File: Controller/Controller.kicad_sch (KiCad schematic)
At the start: 27 parts, among them SW1 SW_DPST_x2, SW2 SW_Push, SW3 SW_Push, SW4 SW_Push, SW5 SW_Push, SW6 SW_Push, SW7 SW_Push, SW8 SW_Push, SW9 SW_Push

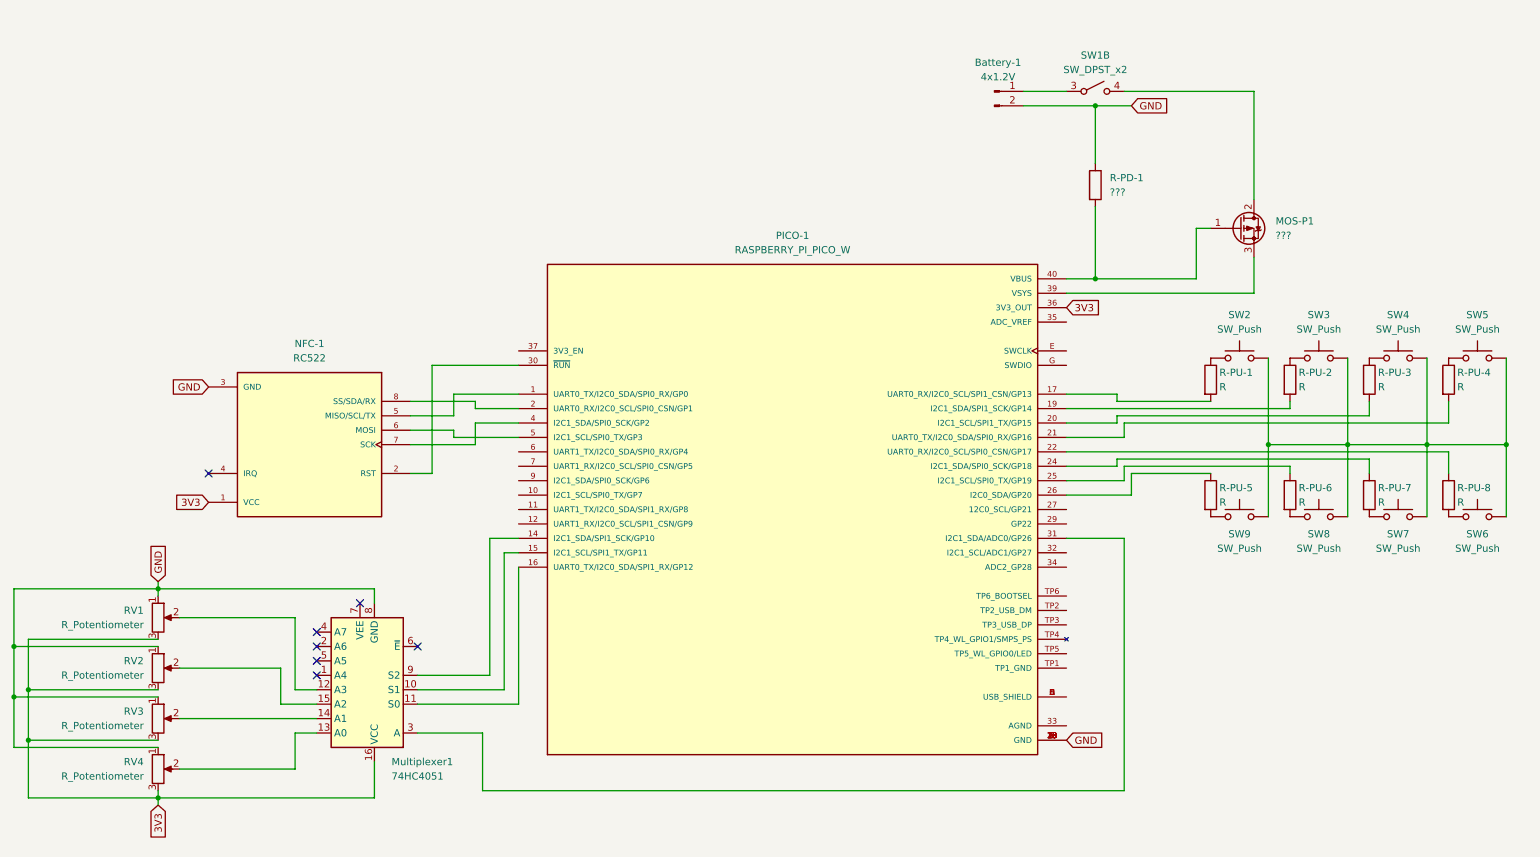
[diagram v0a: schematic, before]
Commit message: Add LEDs and fix button pull up resistors
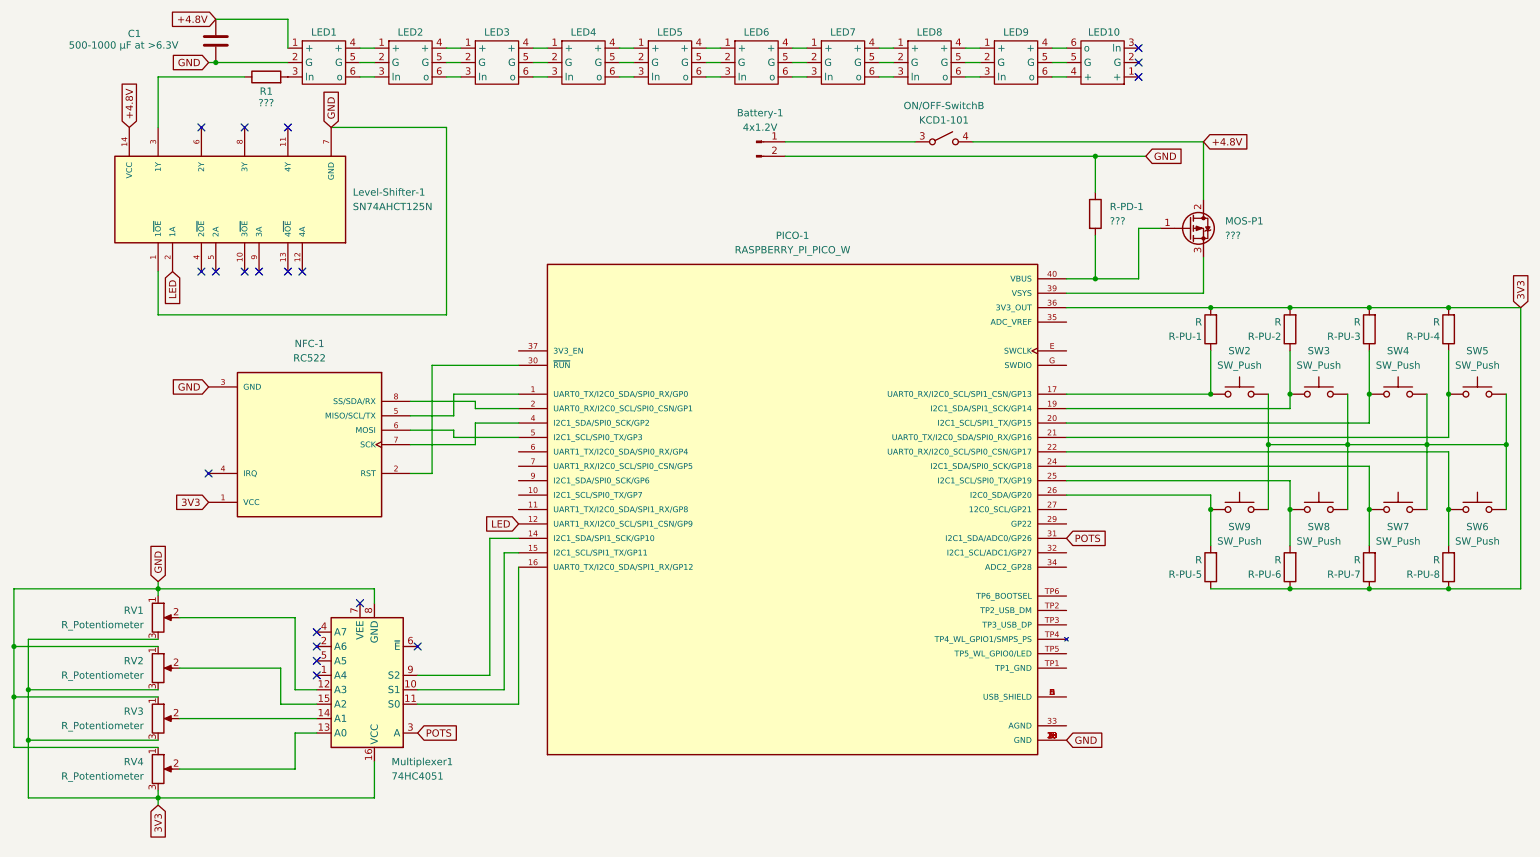
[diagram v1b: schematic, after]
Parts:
- added C1: 500-1000 μF at >6.3V, symbol Device:C
- added LED1, LED10, LED2, LED3, LED4, LED5, LED6, LED7, LED8, LED9: ~, symbol neopixel:neopixel_rgb_pcb
- added Level-Shifter-1: SN74AHCT125N, SN74AHCT125N:DIP794W45P254L1930H508Q14, symbol SN74AHCT125N:SN74AHCT125N
- added R1: ???, symbol Device:R
- NFC-1: footprint Connector_PinHeader_1.00mm:PinHeader_1x08_P1.00mm_Vertical -> CEG006900:MODULE_CEG006900
- ON/OFF-Switch: renamed from SW1; value SW_DPST_x2 -> KCD1-101
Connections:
- net 3V3: now also R-PU-1.2, R-PU-2.2, R-PU-3.2, R-PU-4.2, R-PU-5.1, R-PU-6.1, R-PU-7.1, R-PU-8.1
- net GND: now also C1.2, LED1.2 (G), Level-Shifter-1.1 (1~{OE}), Level-Shifter-1.7 (GND)
- net LED: now reaches PICO-1.12 (UART1_RX/I2C0_SCL/SPI1_CSN/GP9)
- net LED: now also Level-Shifter-1.2 (1A)
- net at PICO-1.17 (UART0_RX/I2C0_SCL/SPI1_CSN/GP13): now also R-PU-1.1, SW2.1; no longer R-PU-1.2
- net at PICO-1.19 (I2C1_SDA/SPI1_SCK/GP14): now also R-PU-2.1, SW3.1; no longer R-PU-2.2
- net at PICO-1.20 (I2C1_SCL/SPI1_TX/GP15): now also R-PU-3.1, SW4.1; no longer R-PU-3.2
- net at PICO-1.21 (UART0_TX/I2C0_SDA/SPI0_RX/GP16): now also R-PU-4.1, SW5.1; no longer R-PU-4.2
- net at PICO-1.22 (UART0_RX/I2C0_SCL/SPI0_CSN/GP17): now also R-PU-8.2, SW6.1; no longer R-PU-8.1
- net at PICO-1.24 (I2C1_SDA/SPI0_SCK/GP18): now also R-PU-7.2, SW7.1; no longer R-PU-7.1
- net at PICO-1.25 (I2C1_SCL/SPI0_TX/GP19): now also R-PU-6.2, SW8.1; no longer R-PU-6.1
- net at PICO-1.26 (I2C0_SDA/GP20): now also R-PU-5.2, SW9.1; no longer R-PU-5.1
- net POTS: now reaches Multiplexer1.3 (A), PICO-1.31 (I2C1_SDA/ADC0/GP26)
- net +4.8V: now reaches MOS-P1.2 (D), ON/OFF-Switch.4 (B)
- net +4.8V: now also C1.1, LED1.1 (+), Level-Shifter-1.14 (VCC)
- new net: Level-Shifter-1.3 (1Y), R1.1
- new net: LED1.3 (ln), R1.2
- new net: LED10.4 (+), LED9.6 (o)
- new net: LED10.5 (G), LED9.5 (G)
- new net: LED10.6 (o), LED9.4 (+)
- new net: LED2.4 (+), LED3.1 (+)
- new net: LED2.5 (G), LED3.2 (G)
- new net: LED2.6 (o), LED3.3 (ln)
- new net: LED3.4 (+), LED4.1 (+)
- new net: LED3.5 (G), LED4.2 (G)
- new net: LED3.6 (o), LED4.3 (ln)
- new net: LED4.4 (+), LED5.1 (+)
- new net: LED4.5 (G), LED5.2 (G)
- new net: LED4.6 (o), LED5.3 (ln)
- new net: LED5.4 (+), LED6.1 (+)
- new net: LED5.5 (G), LED6.2 (G)
- new net: LED5.6 (o), LED6.3 (ln)
- new net: LED8.4 (+), LED9.1 (+)
- new net: LED8.5 (G), LED9.2 (G)
- new net: LED8.6 (o), LED9.3 (ln)
- new net: LED6.4 (+), LED7.1 (+)
- new net: LED6.5 (G), LED7.2 (G)
- new net: LED6.6 (o), LED7.3 (ln)
- new net: LED7.4 (+), LED8.1 (+)
- new net: LED7.5 (G), LED8.2 (G)
- new net: LED7.6 (o), LED8.3 (ln)
- new net: LED1.4 (+), LED2.1 (+)
- new net: LED1.5 (G), LED2.2 (G)
- new net: LED1.6 (o), LED2.3 (ln)
- no-connect marks 7 -> 19
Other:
- company: (none) -> ETIMC
- title: (none) -> Controller
- moved on the sheet: Battery-1, MOS-P1, ON/OFF-SwitchB, R-PD-1, R-PU-1, R-PU-2, R-PU-3, R-PU-4, R-PU-5, R-PU-6, R-PU-7, R-PU-8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
